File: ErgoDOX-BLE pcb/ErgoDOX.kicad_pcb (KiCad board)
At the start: 2 copper layers, 182.8 x 158.9 mm, 115 parts, among them J1 Conn_01x04, J2 Conn_01x02_Female, J3 Conn_01x02_Female, J4 Conn_01x02, J5 Conn_01x02, P1 USB_C_Plug_USB2.0, Q1 Q_NPN_BCE, SW0:10 SW0:3, SW0:11 SW0:2, SW0:12 SW0:1, SW0:7 SW0:6, SW0:8 SW0:5, SW0:9 SW0:4, SW1:10 SW1:3, SW1:11 SW1:2, SW1:12 SW1:1, SW1:13 SW1:0, SW1:9 SW1:4, SW2:10 SW2:3, SW2:11 SW2:2, SW2:12 SW2:1, SW2:13 SW2:0, SW2:7 SW2:6, SW2:8 SW2:5, SW2:9 SW2:4, SW3:10 SW3:3, SW3:11 SW3:2, SW3:12 SW3:1, SW3:13 SW3:0, SW3:8 SW3:5, SW3:9 SW3:4, SW4:10 SW4:3, SW4:11 SW4:2, SW4:12 SW4:1, SW4:13 SW4:0, SW4:7 SW4:6, SW4:8 SW4:5, SW4:9 SW4:4, SW5:10 SW5:3, SW5:11 SW5:2, SW5:12 SW5:1, SW5:13 SW5:0, SW5:7 SW5:6, SW5:8 SW5:5, SW5:9 SW5:4, U1 MCP23018, U3 C0720B001F

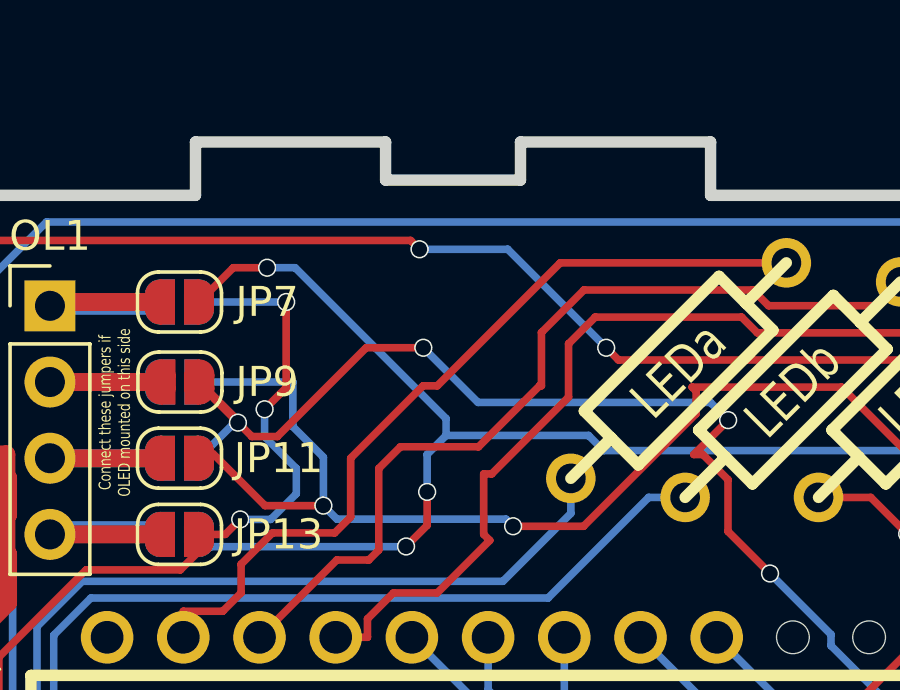
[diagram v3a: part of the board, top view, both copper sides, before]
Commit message: Do initial placement of TRRS jack
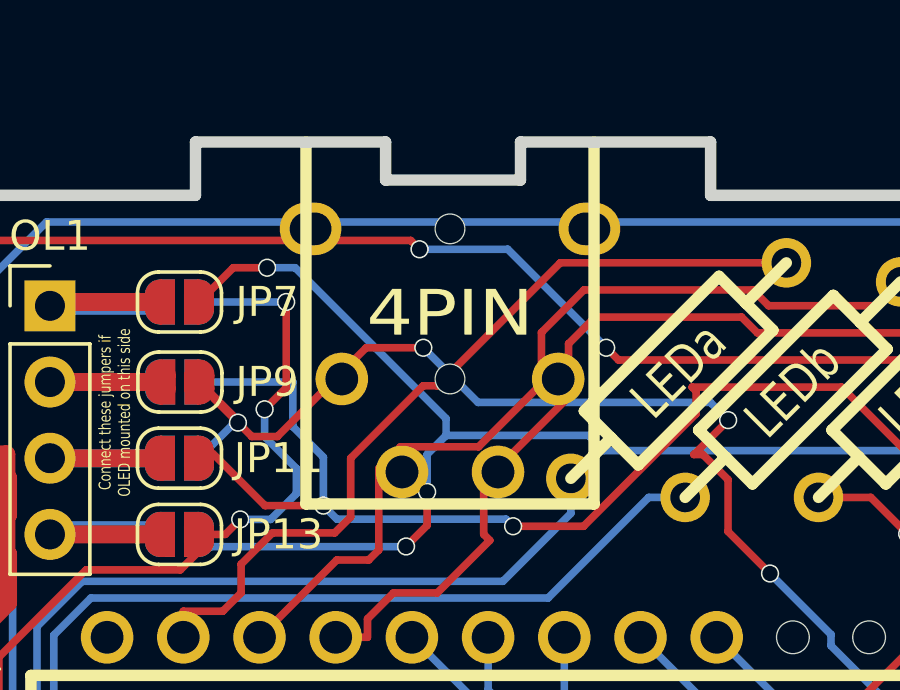
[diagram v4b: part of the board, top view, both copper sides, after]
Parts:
- added J6: 4PIN, ErgoDOX pcb:4pin35mmAudio, F.Cu at (80.0, 36.8)
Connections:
- D1:7 pad 2: /COL5 -> /COL6
- SX0:10 pad 1: /COL5 -> /ROW0
- SX0:10 pad 2: /COL5 -> Net-(SW0:10-Pad2)
- SX0:11 pad 1: /COL5 -> /ROW0
- SX1:7 pad 1: /COL5 -> /ROW1
- SX1:8 pad 1: /COL5 -> /ROW1
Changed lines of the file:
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@@
       (solder_mask_margin -0.254) (zone_connect 2))
     (pad "1" thru_hole circle locked (at 2.54 -5.08 25) (size 2.286 2.286) (drill 1.4986) (layers *.Cu *.SilkS *.Mask)
-      (net 4 "/COL5") (pinfunction "1") (pintype "passive"))
+      (net 10 "/ROW1") (pinfunction "1") (pintype "passive"))
     (pad "1" thru_hole circle locked (at 3.81 -2.54 25) (size 2.286 2.286) (drill 1.4986) (layers *.Cu *.SilkS *.Mask)
-      (net 4 "/COL5") (pinfunction "1") (pintype "passive"))
+      (net 10 "/ROW1") (pinfunction "1") (pintype "passive"))
     (pad "2" thru_hole circle locked (at -3.81 -2.54 25) (size 2.286 2.286) (drill 1.4986) (layers *.Cu *.SilkS *.Mask)
       (net 18 "Net-(D1:8-Pad1)") (pinfunction "2") (pintype "passive"))
@@
       (solder_mask_margin -0.254) (zone_connect 2))
     (pad "1" thru_hole circle locked (at 2.54 -5.08 25) (size 2.286 2.286) (drill 1.4986) (layers *.Cu *.SilkS *.Mask)
-      (net 4 "/COL5") (pinfunction "1") (pintype "passive"))
+      (net 10 "/ROW1") (pinfunction "1") (pintype "passive"))
     (pad "1" thru_hole circle locked (at 3.81 -2.54 25) (size 2.286 2.286) (drill 1.4986) (layers *.Cu *.SilkS *.Mask)
-      (net 4 "/COL5") (pinfunction "1") (pintype "passive"))
+      (net 10 "/ROW1") (pinfunction "1") (pintype "passive"))
     (pad "2" thru_hole circle locked (at -3.81 -2.54 25) (size 2.286 2.286) (drill 1.4986) (layers *.Cu *.SilkS *.Mask)
       (net 17 "Net-(D1:7-Pad1)") (pinfunction "2") (pintype "passive"))
@@
       (solder_mask_margin -0.254) (zone_connect 2))
     (pad "1" thru_hole circle locked (at 3.81 -2.54 205) (size 2.286 2.286) (drill 1.4986) (layers *.Cu *.SilkS *.Mask)
-      (net 4 "/COL5") (pinfunction "1") (pintype "passive"))
+      (net 9 "/ROW0") (pinfunction "1") (pintype "passive"))
     (pad "1" thru_hole circle locked (at 2.54 -5.08 205) (size 2.286 2.286) (drill 1.4986) (layers *.Cu *.SilkS *.Mask)
-      (net 4 "/COL5") (pinfunction "1") (pintype "passive"))
+      (net 9 "/ROW0") (pinfunction "1") (pintype "passive"))
     (pad "2" thru_hole circle locked (at -2.54 -5.08 205) (size 2.286 2.286) (drill 1.4986) (layers *.Cu *.SilkS *.Mask)
-      (net 4 "/COL5") (pinfunction "2") (pintype "passive"))
+      (net 25 "Net-(SW0:10-Pad2)") (pinfunction "2") (pintype "passive"))
     (pad "2" thru_hole circle locked (at -3.81 -2.54 205) (size 2.286 2.286) (drill 1.4986) (layers *.Cu *.SilkS *.Mask)
-      (net 4 "/COL5") (pinfunction "2") (pintype "passive"))
+      (net 25 "Net-(SW0:10-Pad2)") (pinfunction "2") (pintype "passive"))
   )
   (footprint "MX_FLIP" (layer "F.Cu")
@@
       (solder_mask_margin -0.254) (zone_connect 2))
     (pad "1" thru_hole circle locked (at 3.81 -2.54 205) (size 2.286 2.286) (drill 1.4986) (layers *.Cu *.SilkS *.Mask)
-      (net 4 "/COL5") (pinfunction "1") (pintype "passive"))
+      (net 9 "/ROW0") (pinfunction "1") (pintype "passive"))
     (pad "1" thru_hole circle locked (at 2.54 -5.08 205) (size 2.286 2.286) (drill 1.4986) (layers *.Cu *.SilkS *.Mask)
-      (net 4 "/COL5") (pinfunction "1") (pintype "passive"))
+      (net 9 "/ROW0") (pinfunction "1") (pintype "passive"))
     (pad "2" thru_hole circle locked (at -2.54 -5.08 205) (size 2.286 2.286) (drill 1.4986) (layers *.Cu *.SilkS *.Mask)
       (net 26 "Net-(SW0:11-Pad2)") (pinfunction "2") (pintype "passive"))
@@
       (net 17 "Net-(D1:7-Pad1)") (pinfunction "A") (pintype "passive"))
     (pad "2" thru_hole rect locked (at 3.81 0 25) (size 1.651 1.651) (drill 0.9906) (layers *.Cu *.SilkS *.Mask)
-      (net 4 "/COL5") (pinfunction "K") (pintype "passive"))
+      (net 5 "/COL6") (pinfunction "K") (pintype "passive"))
     (pad "99" smd rect locked (at 1.6637 0 25) (size 0.8382 0.8382) (layers "B.Cu" "B.Paste" "B.Mask"))
     (pad "99" smd rect locked (at -1.6637 0 25) (size 0.8382 0.8382) (layers "F.Cu" "F.Paste" "F.Mask"))
@@
       ))
   )
+  (footprint "ErgoDOX pcb:4pin35mmAudio" (layer "F.Cu")
+    (at 80.01 36.83)
+    (property "Sheetfile" "ErgoDOX.kicad_sch")
+    (property "Sheetname" "")
+    (attr through_hole)
+    (fp_text reference "J6" (at 1.27 0 90) (layer "F.SilkS") hide
+      (effects (font (size 1.524 1.778) (thickness 0.3048)))
+    )
+    (fp_text value "4PIN" (at 6.35 -0.635) (layer "F.SilkS")
+      (effects (font (size 1.524 1.778) (thickness 0.3048)))
+    )
+    (fp_text user "3.5mm" (at 6.35 -0.635) (layer "B.SilkS")
+      (effects (font (size 1.524 1.778) (thickness 0.3048)) (justify mirror))
+    )
+    (fp_line (start 11.1506 5.715) (end 1.5494 5.715) (layer "B.SilkS") (width 0.381))
+    (fp_line (start 11.1506 -6.35) (end 11.1506 5.715) (layer "B.SilkS") (width 0.381))
+    (fp_line (start 1.5494 5.715) (end 1.5494 -6.35) (layer "B.SilkS") (width 0.381))
+    (fp_line (start 11.1506 5.715) (end 1.5494 5.715) (layer "F.SilkS") (width 0.381))
+    (fp_line (start 11.1506 -6.35) (end 11.1506 5.715) (layer "F.SilkS") (width 0.381))
+    (fp_line (start 1.5494 5.715) (end 1.5494 -6.35) (layer "F.SilkS") (width 0.381))
+    (fp_line (start 8.5979 -6.35) (end 8.5979 -5.0546) (layer "Dwgs.User") (width 0.381))
+    (fp_line (start 11.1506 -6.35) (end 8.5979 -6.35) (layer "Dwgs.User") (width 0.381))
+    (fp_line (start 4.1021 -5.0546) (end 4.1021 -6.35) (layer "Dwgs.User") (width 0.381))
+    (fp_line (start 11.1506 5.715) (end 11.1506 -6.35) (layer "Dwgs.User") (width 0.381))
+    (fp_line (start 8.5979 -5.0546) (end 4.1021 -5.0546) (layer "Dwgs.User") (width 0.381))
+    (fp_line (start 6.35 -6.35) (end 6.35 -6.35) (layer "Dwgs.User") (width 0.0254))
+    (fp_line (start 4.1021 -6.35) (end 1.5494 -6.35) (layer "Dwgs.User") (width 0.381))
+    (fp_line (start 1.5494 -6.35) (end 1.5494 5.715) (layer "Dwgs.User") (width 0.381))
+    (fp_line (start 1.5494 5.715) (end 11.1506 5.715) (layer "Dwgs.User") (width 0.381))
+    (fp_line (start 8.5979 -6.35) (end 11.1506 -6.35) (layer "Cmts.User") (width 0.381))
+    (fp_line (start 8.5979 -6.35) (end 8.5979 -5.0546) (layer "Cmts.User") (width 0.381))
+    (fp_line (start 4.1021 -5.0546) (end 4.1021 -6.35) (layer "Cmts.User") (width 0.381))
+    (fp_line (start 8.5979 -5.0546) (end 4.1021 -5.0546) (layer "Cmts.User") (width 0.381))
+    (fp_line (start 1.5494 -6.35) (end 4.1021 -6.35) (layer "Cmts.User") (width 0.381))
+    (pad "" np_thru_hole circle (at 6.35 1.5494 270) (size 0.9906 0.9906) (drill 0.9906) (layers *.Cu *.Mask "F.SilkS"))
+    (pad "" np_thru_hole circle (at 6.35 -3.4544 270) (size 0.9906 0.9906) (drill 0.9906) (layers *.Cu *.Mask "F.SilkS"))
+    (pad "1" thru_hole oval (at 10.9982 -3.4544 270) (size 1.7526 2.0574) (drill oval 1.0922 1.397) (layers *.Cu *.Mask "F.SilkS")
+      (net 104 "/OLED_P1") (pinfunction "1") (pintype "input"))
+    (pad "2" thru_hole circle (at 2.7432 1.5494 270) (size 1.7526 1.7526) (drill 1.0922) (layers *.Cu *.Mask "F.SilkS")
+      (net 105 "/OLED_P2") (pinfunction "2") (pintype "power_in"))
+    (pad "3" thru_hole circle (at 7.9502 4.6482 270) (size 1.7526 1.7526) (drill 1.0922) (layers *.Cu *.Mask "F.SilkS")
+      (net 106 "/OLED_P3") (pinfunction "3") (pintype "output"))
+    (pad "4" thru_hole oval (at 1.7018 -3.4544 270) (size 1.7526 2.0574) (drill oval 1.0922 1.397) (layers *.Cu *.Mask "F.SilkS")
+      (net 107 "/OLED_P4") (pinfunction "4") (pintype "power_in"))
+    (pad "5" thru_hole circle (at 4.7498 4.6482 270) (size 1.7526 1.7526) (drill 1.0922) (layers *.Cu *.Mask "F.SilkS"))
+    (pad "6" thru_hole circle (at 9.9568 1.5494 270) (size 1.7526 1.7526) (drill 1.0922) (layers *.Cu *.Mask "F.SilkS"))
+  )
   (footprint "" (layer "F.Cu")

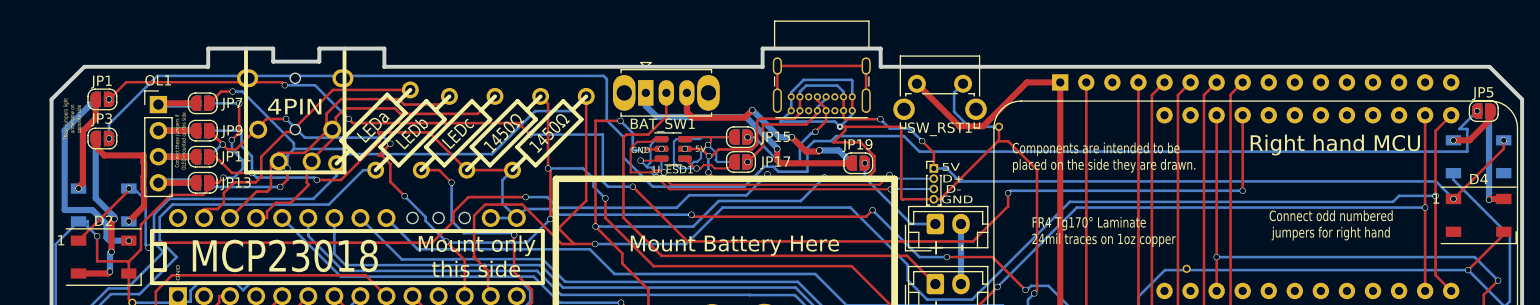
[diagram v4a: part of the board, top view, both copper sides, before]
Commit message: Added audio jack and traces
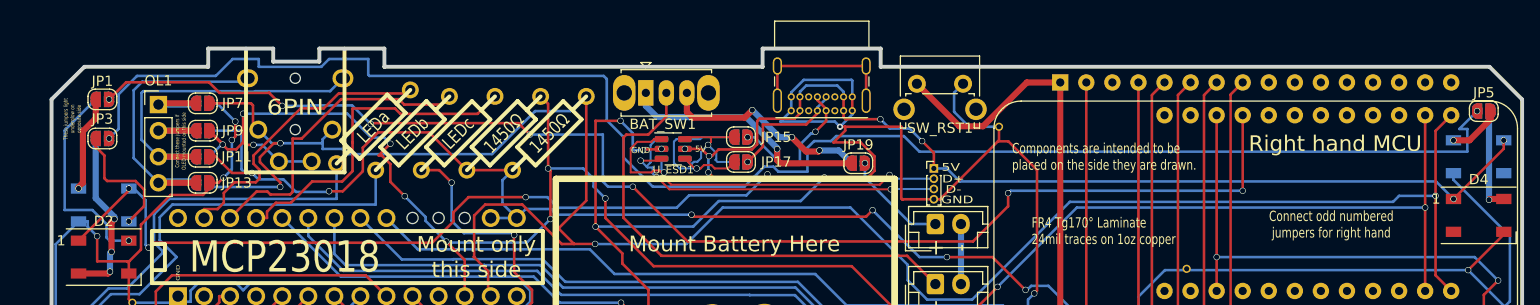
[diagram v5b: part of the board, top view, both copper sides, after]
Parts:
- J6: value 4PIN -> 6PIN
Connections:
- J6 pad 1: /OLED_P1 -> /OLED_P3
- J6 pad 2: /OLED_P2 -> /SDA
- J6 pad 3: /OLED_P3 -> /SCL
- J6 pad 5: (no net) -> /SCL
- J6 pad 6: (no net) -> /SDA
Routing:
- net /OLED_P3: track 7.34 -> 34.5 mm
- net /OLED_P4: track 7.19 -> 28.8 mm
- net /SCL: track 180.3 -> 190.1 mm, vias 10 -> 11
- net Net-(JP3-Pad2): track 153.6 -> 158.1 mm
- net /SDA: track 202.3 -> 205.5 mm, vias 5 -> 4
- net GND: track 696.8 -> 693.7 mm
- net +3V3: track 311.6 -> 313.6 mm
- net Net-(LED_B1-Pad1): track 78.4 -> 80.3 mm
- net Net-(LED_A1-Pad1): track 62.7 -> 64.0 mm
- net /LED_A: track 27.5 -> 28.5 mm
- net /LED_C: track 31.6 -> 32.6 mm
- net Net-(D1-Pad2): track 12.9 -> 12.3 mm
- net /LED_B: track 29.3 -> 30.0 mm

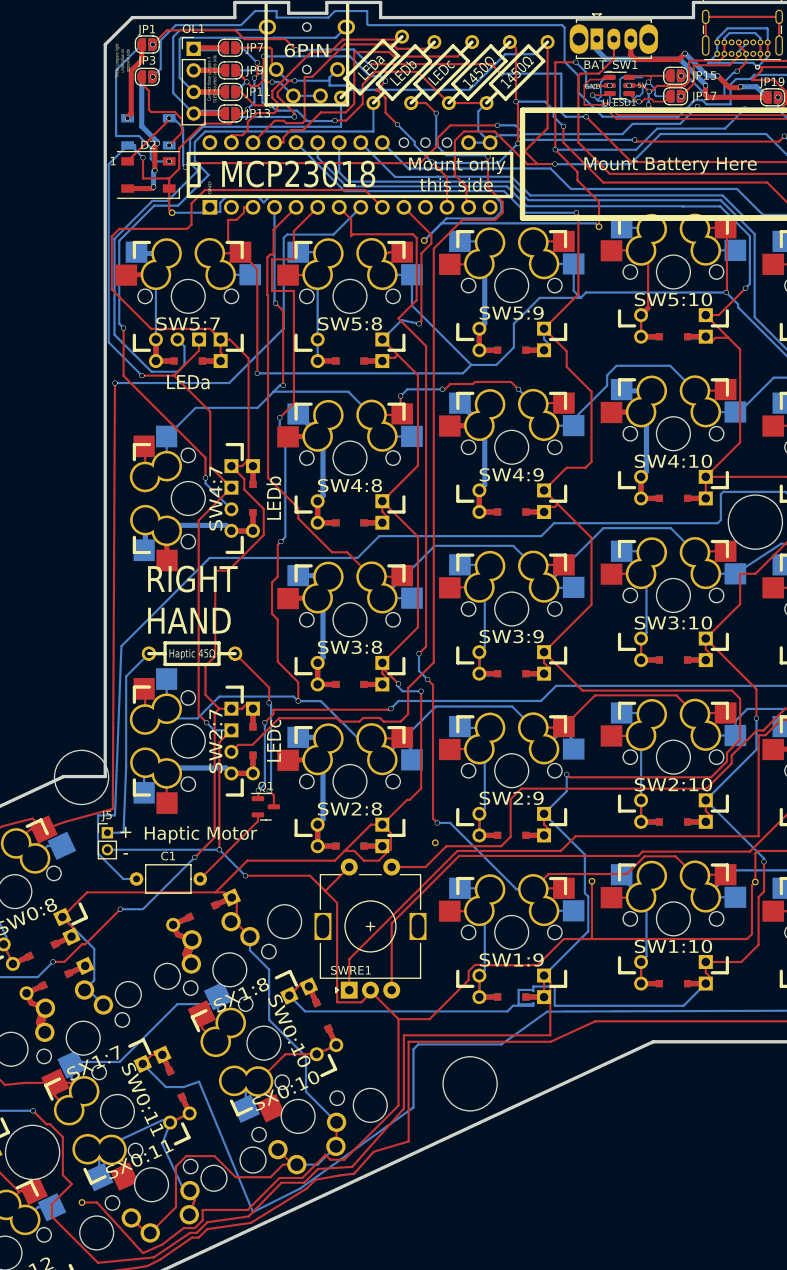
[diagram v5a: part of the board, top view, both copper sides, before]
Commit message: Fixing some of the clearance issues
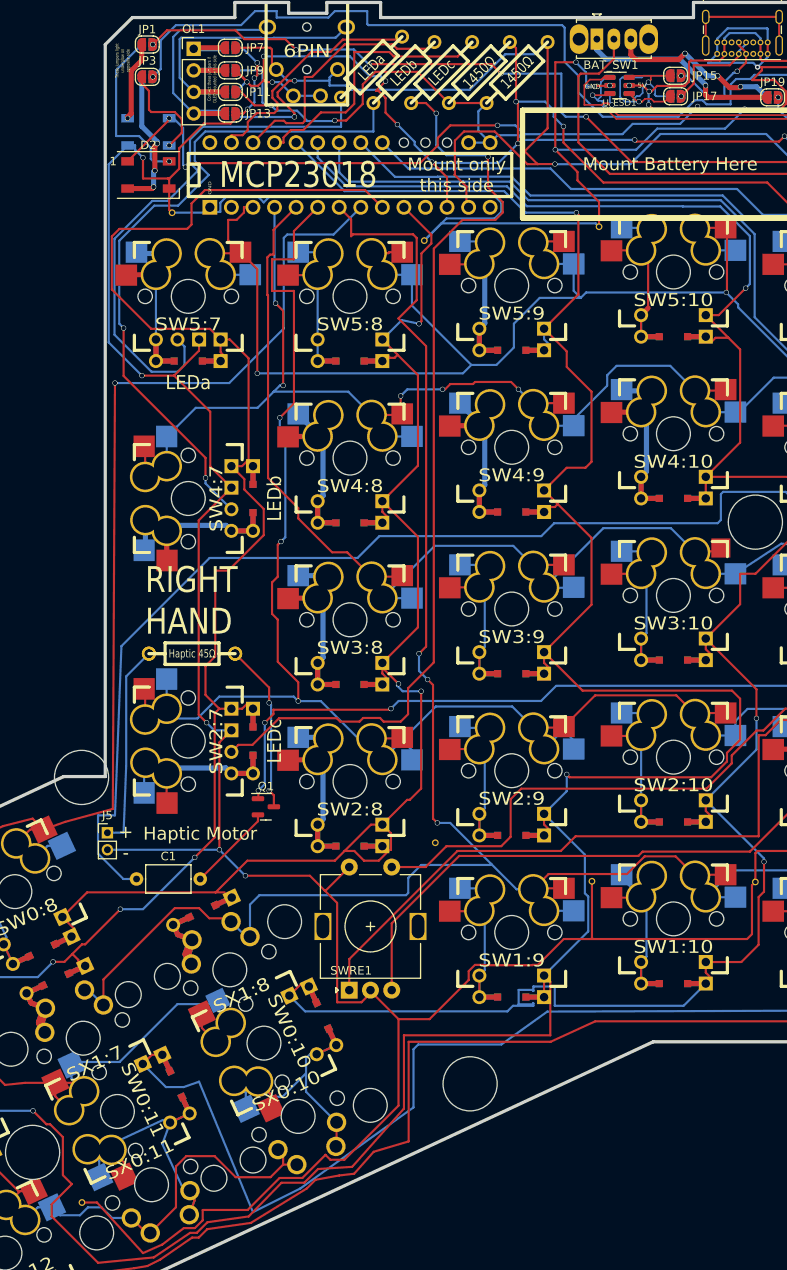
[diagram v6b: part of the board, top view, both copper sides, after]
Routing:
- net /COL5: track 235.6 -> 150.7 mm
- net /ROW1: track 224.0 -> 286.8 mm
- net /ROW0: track 252.5 -> 293.6 mm
- net Net-(SW0:10-Pad2): track 24.5 -> 37.2 mm
- net /COL6: track 175.9 -> 177.1 mm

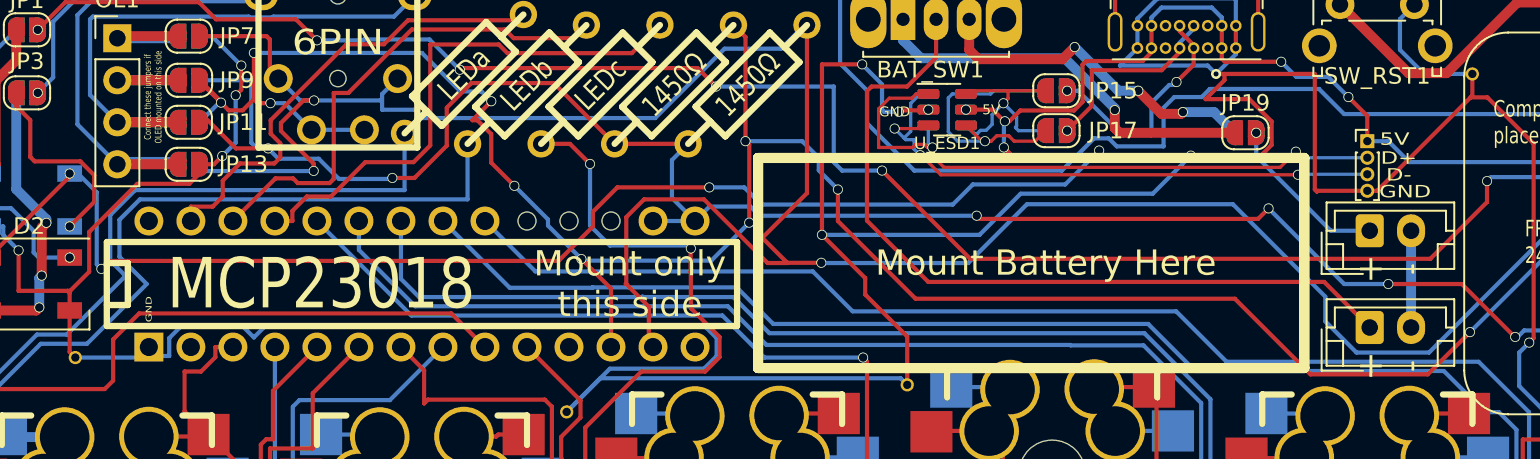
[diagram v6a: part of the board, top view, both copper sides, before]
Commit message: Add jumpers for setting address of IO expander
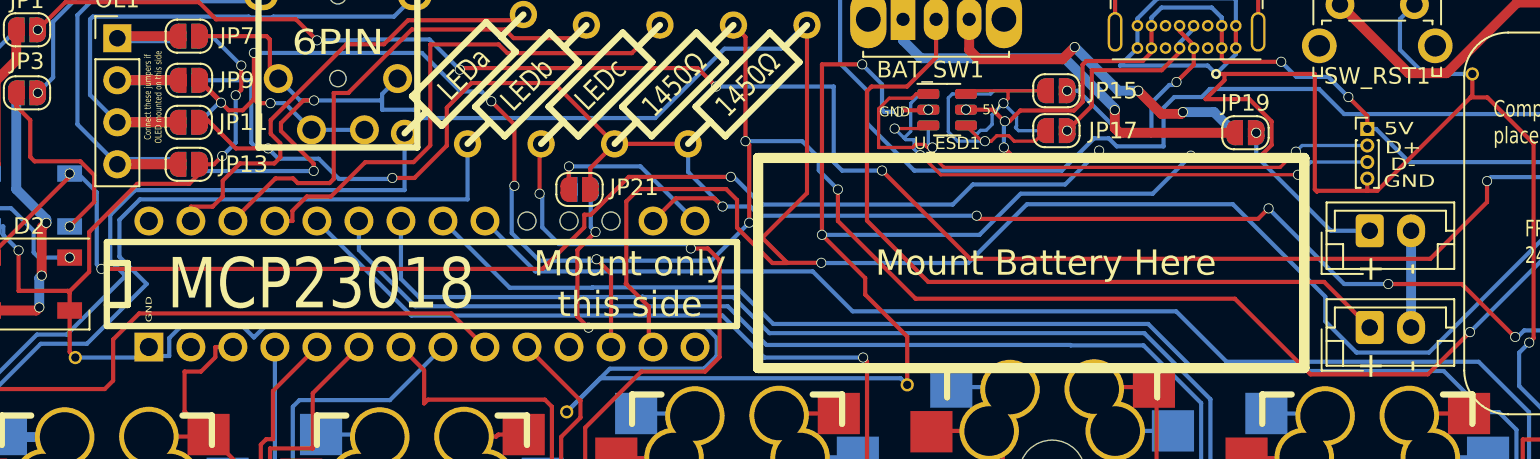
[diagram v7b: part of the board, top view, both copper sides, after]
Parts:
- added JP21: SolderJumper_2_Open, Jumper:SolderJumper-2_P1.3mm_Open_RoundedPad1.0x1.5mm, F.Cu at (101.0, 45.1)
- added JP22: SolderJumper_2_Open, Jumper:SolderJumper-2_P1.3mm_Open_RoundedPad1.0x1.5mm, B.Cu at (101.0, 45.1)
- moved J1 0.74 mm to (148.6, 41.4)
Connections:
- U1 pad 15: +3V3 -> /MCP23018_ADDR_Selector
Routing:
- net /MCP23018_ADDR_Selector: track 0.00 -> 11.8 mm, vias 0 -> 1
- net GND: track 693.7 -> 703.7 mm, vias 16 -> 18
- net +3V3: track 313.6 -> 316.4 mm, vias 7 -> 8
- net /SDA: track 205.5 -> 207.5 mm
- net Net-(LED_C1-Pad1): track 110.5 -> 111.9 mm
